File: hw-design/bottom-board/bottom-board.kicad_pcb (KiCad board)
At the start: 2 copper layers, 172 x 140.5 mm, 257 parts, among them J1 JACK_TRS_6PINS, J2 JACK_TRS_6PINS, J3 JACK_TRS_6PINS, J4 JACK_TRS_6PINS, J5 JACK_TRS_6PINS, J6 RJ45_LEDS, K1 IM06TS, K2 IM06TS, P1 USB_B, P2 USB_A, P3 DIN_5, P4 DIN_5, P5 BARREL_JACK, P6 HMI_POWER, P7 SD_CARD, P8 HMI_DATA, P9 SERIAL_DEBUG, Q1 2N7002, Q10 2N7002, Q12 2N7002, Q13 2N7002, Q14 BSS84, Q15 BSS84, Q2 2N7002, Q3 J112, Q4 J112, Q5 J112, Q6 J112, Q7 2N7002, Q8 2N7002, Q9 2N7002, SW1 SW_PUSH, U1 MURATA 5V, U10 RT9701, U11 6N137S, U12 ISL83491, U2 NCP1117DT50G, U3 CS4245, U4 AT24CS08-STUM, U5 Core_AW204x, U6 LM4562, U7 LM4562, U8 LM4562, U9 LM4811

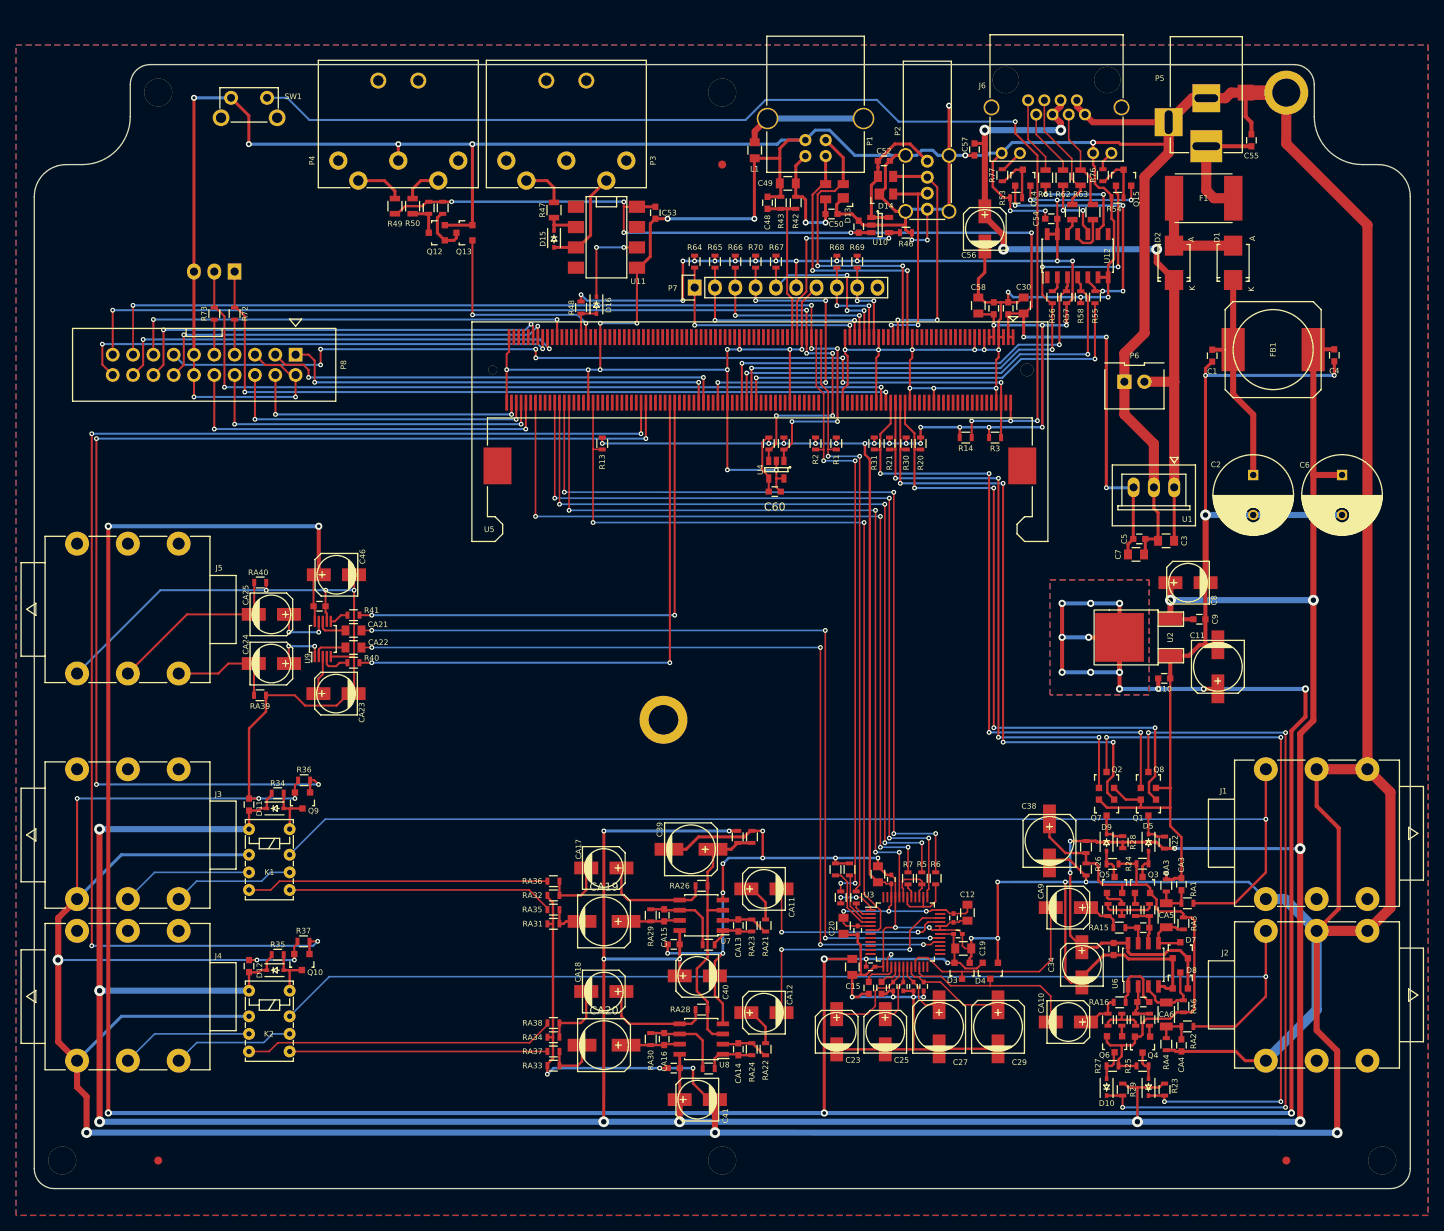
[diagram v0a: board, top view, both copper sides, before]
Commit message: Changed SODIM to Marsboard header + added liniar regulator for audio codec
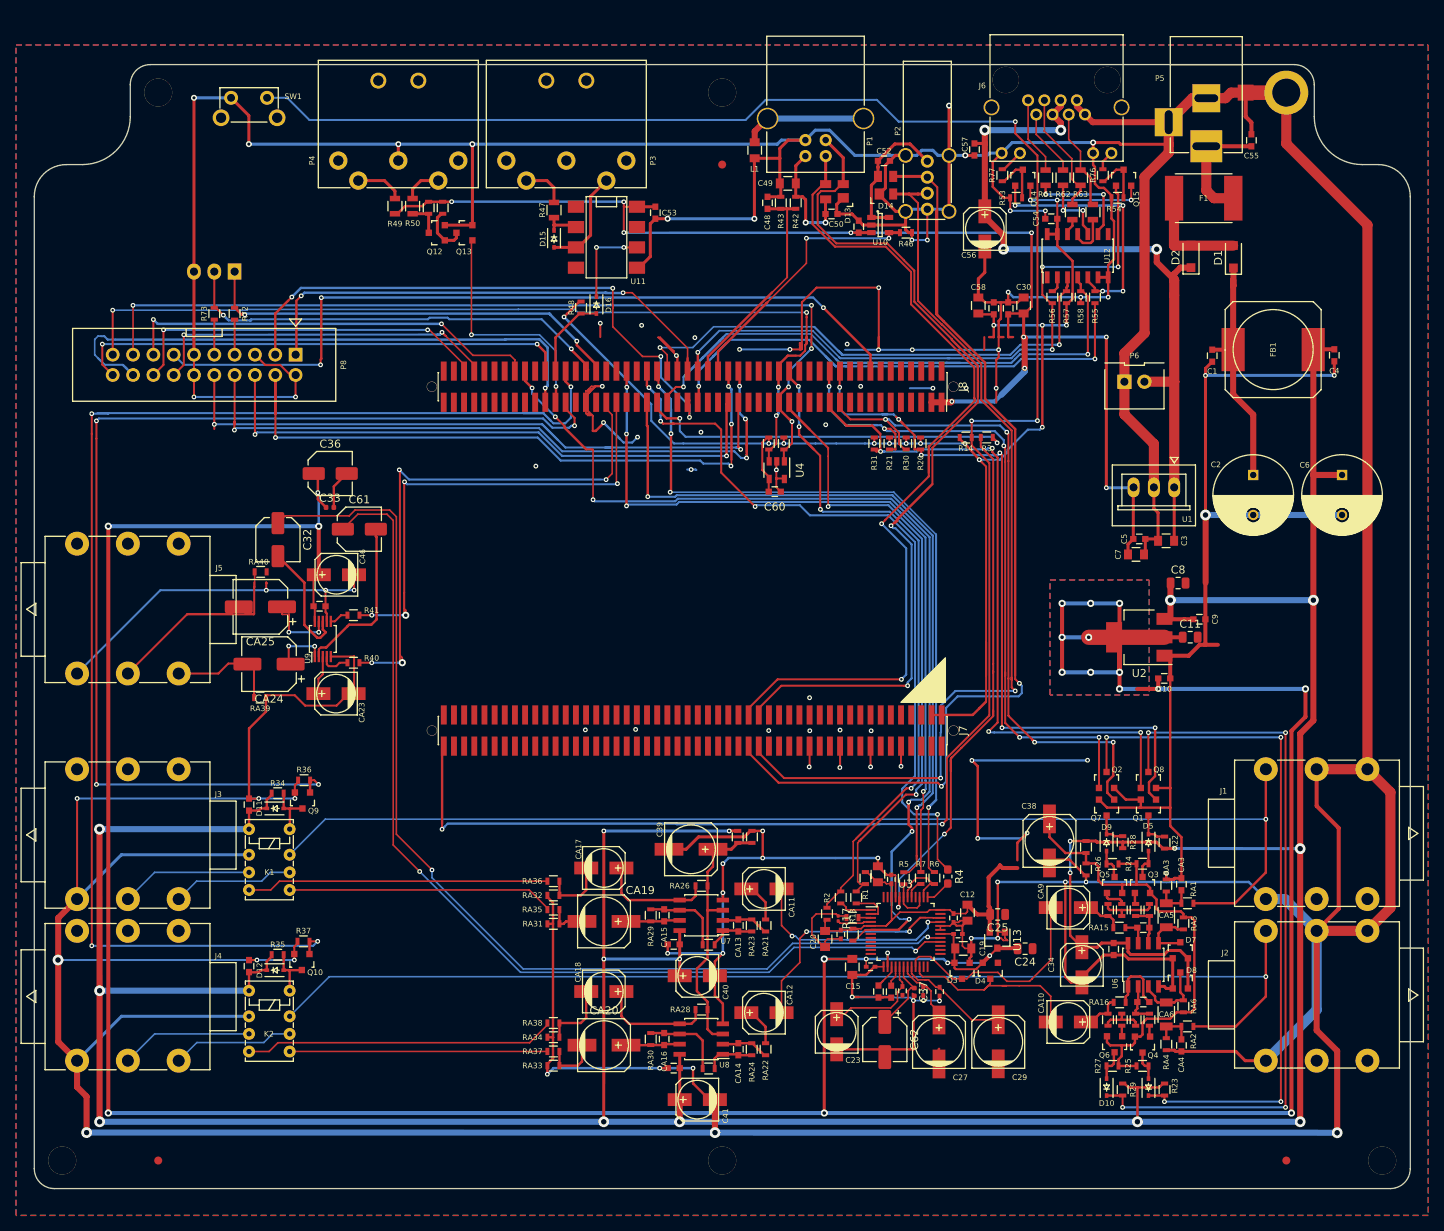
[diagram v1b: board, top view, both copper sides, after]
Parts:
- removed CA21, CA22: 1uF, Capacitors_SMD:C_0805
- removed H6: Standoff, footprints:9774027151R
- removed P7: SD_CARD, Pin_Headers:Pin_Header_Straight_1x10
- removed R11, R64, R65, R66, R67, R68, R69, R70: 10k, Resistors_SMD:R_0603
- removed U5: Core_AW204x, footprints:Socket_SODIMM_DDR3_TE_2013289
- added C32: 10uF, Capacitor_SMD:C_Elec_5x5.4, F.Cu at (90.5, 79.0)
- added C33: 100nF, Capacitor_SMD:C_0402_1005Metric, F.Cu at (97.0, 74.9)
- added C36: 10uF, Capacitor_SMD:C_Elec_5x5.4, F.Cu at (97.1, 70.7)
- added C37: 100nF, Capacitor_SMD:C_0402_1005Metric, F.Cu at (170.1, 135.5)
- added C61: 10uF, Capacitor_SMD:C_Elec_5x5.4, F.Cu at (100.7, 77.6)
- added C62: 10uF, Capacitor_SMD:CP_Elec_5x5.3, F.Cu at (166.4, 141.4)
- added G***: LOGO, footprints:mod-logo, B.Cu at (145.7, 91.9)
- added J7: Conn_02x50_Odd_Even, footprints-local:Pin_Header_Straight_2x50_Pitch1.27mm_SMD, F.Cu at (142.4, 102.8)
- added J8: Conn_02x50_Odd_Even, footprints-local:Pin_Header_Straight_2x50_Pitch1.27mm_SMD, F.Cu at (142.4, 59.8)
- added R17: 10k, Resistor_SMD:R_0201_0603Metric, F.Cu at (160.6, 126.3)
- added R4: 22R, Resistor_SMD:R_0603_1608Metric_Pad1.05x0.95mm_HandSolder, F.Cu at (174.3, 121.1)
- added U13: AP2120N-3.3, Package_TO_SOT_SMD:SOT-23, F.Cu at (180.5, 129.0)
- C11: value 100uF -> 10uF; footprint Capacitors_SMD:c_elec_6.3x5.3 -> Capacitor_SMD:C_0805_2012Metric
- C2, C6: value 1000uF -> 2200uF
- C24: value 100nF -> 1uF; footprint Capacitors_SMD:C_0402 -> Capacitor_SMD:C_0805_2012Metric
- C25, C8: footprint Capacitors_SMD:c_elec_5x5.3 -> Capacitor_SMD:C_0805_2012Metric
- CA24, CA25: value 10uF -> 100uF; footprint Capacitors_SMD:c_elec_5x5.3 -> Capacitor_SMD:CP_Elec_6.3x7.7
- D1, D2: value B130LB -> MBR230; footprint Diodes_SMD:Diode-SMB_Standard -> Diode_SMD:D_SOD-123F
- FB1: value 100uH -> 1mH
- R10, R9: value 100R -> 22R
- R3: value 10k -> 22R
- U2: value NCP1117DT50G -> LD1117S50TR_SOT223; footprint SMD_Packages:DPAK-2 -> Package_TO_SOT_SMD:SOT-223-3_TabPin2
- U3: footprint Housings_QFP:LQFP-48_7x7mm_Pitch0.5mm -> Package_QFP:LQFP-48_7x7mm_P0.5mm
- U4: footprint Housings_SOT-23_SOT-143_TSOT-6:SOT-23-5 -> Package_TO_SOT_SMD:SOT-23-5
- moved R13 68.9 mm to (162.4, 128.3), turned to 270 degrees
- moved R2 58.8 mm to (159.2, 125.7), turned to 270 degrees
- moved R1 54.4 mm to (164.0, 121.3)
- moved C25 20.3 mm to (180.5, 125.8), turned to 180 degrees
- moved C24 15.9 mm to (183.9, 130.1), turned to 180 degrees
- moved R12 6.40 mm to (162.4, 126.2), turned to 0 degrees
- moved C11 5.07 mm to (204.6, 91.1), turned to 0 degrees
- moved U2 3.88 mm to (198.2, 91.2), turned to 180 degrees
- moved CA1 2.84 mm to (167.2, 135.5)
- moved C20 2.83 mm to (158.9, 128.9)
- moved D2 2.27 mm to (204.7, 43.5)
- moved R5 2.25 mm to (168.8, 121.3)
- moved C21 2.17 mm to (160.9, 128.3)
- moved C28 2.09 mm to (173.2, 135.4)
- moved C27 1.89 mm to (173.2, 141.7)
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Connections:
- C12 pad 2: +3V3 -> +3.3VA
- C14 pad 2: +3V3 -> +3.3VA
- C16 pad 2: +3V3 -> +3.3VA
- C18 pad 1: +3V3 -> +3.3VA
- C20 pad 2: +3V3 -> +3.3VA
- C21 pad 2: +3V3 -> +3.3VA
- C24 pad 1: Net-(C24-Pad1) -> GNDA
- C24 pad 2: GNDA -> +5VA
- C25 pad 1: Net-(C24-Pad1) -> GNDA
- C25 pad 2: GNDA -> +3.3VA
- R1 pad 2: +3V3 -> +3.3VA
- R13 pad 1: CODEC_~RESET -> +3.3VA
- R13 pad 2: +3V3 -> CODEC_~RESET
- R2 pad 2: +3V3 -> +3.3VA
- R3 pad 1: +3V3 -> Net-(R3-Pad1)
- R3 pad 2: POWER_BUTTON -> CODEC_I2S_MCLK
- U11 pad 1: (no net) -> Net-(U11-Pad1)
- U11 pad 4: (no net) -> Net-(U11-Pad4)
- U3 pad 15: Net-(CA1-Pad1) -> Net-(CA2-Pad1)
- U3 pad 16: Net-(CA2-Pad1) -> Net-(CA1-Pad1)
- U3 pad 18: Net-(C24-Pad1) -> Net-(C37-Pad1)
- U3 pad 3: Net-(R11-Pad2) -> Net-(R12-Pad2)
- U3 pad 36: +3V3 -> +3.3VA
- U3 pad 37: CODEC_I2S_SDIN -> Net-(R4-Pad2)
- U3 pad 4: Net-(R12-Pad2) -> Net-(R17-Pad2)
- U3 pad 44: CODEC_I2S_MCLK -> Net-(R3-Pad1)
- U3 pad 46: +3V3 -> +3.3VA
- U3 pad 5: +3V3 -> +3.3VA
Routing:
- net UBOOT_BUTTON: track 148.0 -> 280.9 mm, vias 4 -> 5
- net USB_HOST_DM: track 29.7 -> 135.3 mm
- net +3V3: track 292.3 -> 192.7 mm, vias 36 -> 16
- net USB_HOST_DP: track 25.8 -> 116.2 mm
- net USB_DEV_DP: track 38.6 -> 111.0 mm
- net USB_DEV_DM: track 35.3 -> 106.2 mm
- net Net-(R3-Pad1): track 0.00 -> 69.3 mm, vias 0 -> 2
- net CODEC_I2S_MCLK: track 103.1 -> 47.3 mm, vias 4 -> 2
- net HMI_SPI0_MISO: track 35.9 -> 83.2 mm, vias 2 -> 4
- net +3.3VA: track 0.00 -> 46.4 mm
- net CLI_UART_RX: track 99.1 -> 55.7 mm
- net GNDA: track 1685.4 -> 1642.0 mm, vias 77 -> 91
- net CLI_UART_TX: track 97.2 -> 53.9 mm
- net HMI_SPI0_CLK: track 44.7 -> 85.1 mm, vias 2 -> 4
- net SD0_DETECT: track 39.1 -> 0.00 mm, vias 4 -> 0
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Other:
- board text added: "MOD Devices GmbH http://moddevices.com MOD Duo - Bottom Board Rev.: 2019.03.28"
- board text removed: "3V3"
- board text removed: "Musical Operating Devices http://moddevices.com MOD Duo - Bottom Board Rev.: 2016.11.29"
- board text removed: "SD_CLK"
- board text removed: "SD_CMD"
- board text removed: "SD_D0"
- board text removed: "SD_D1"
- board text removed: "SD_D2"
- board text removed: "SD_D3"
- board text removed: "SD_DET"

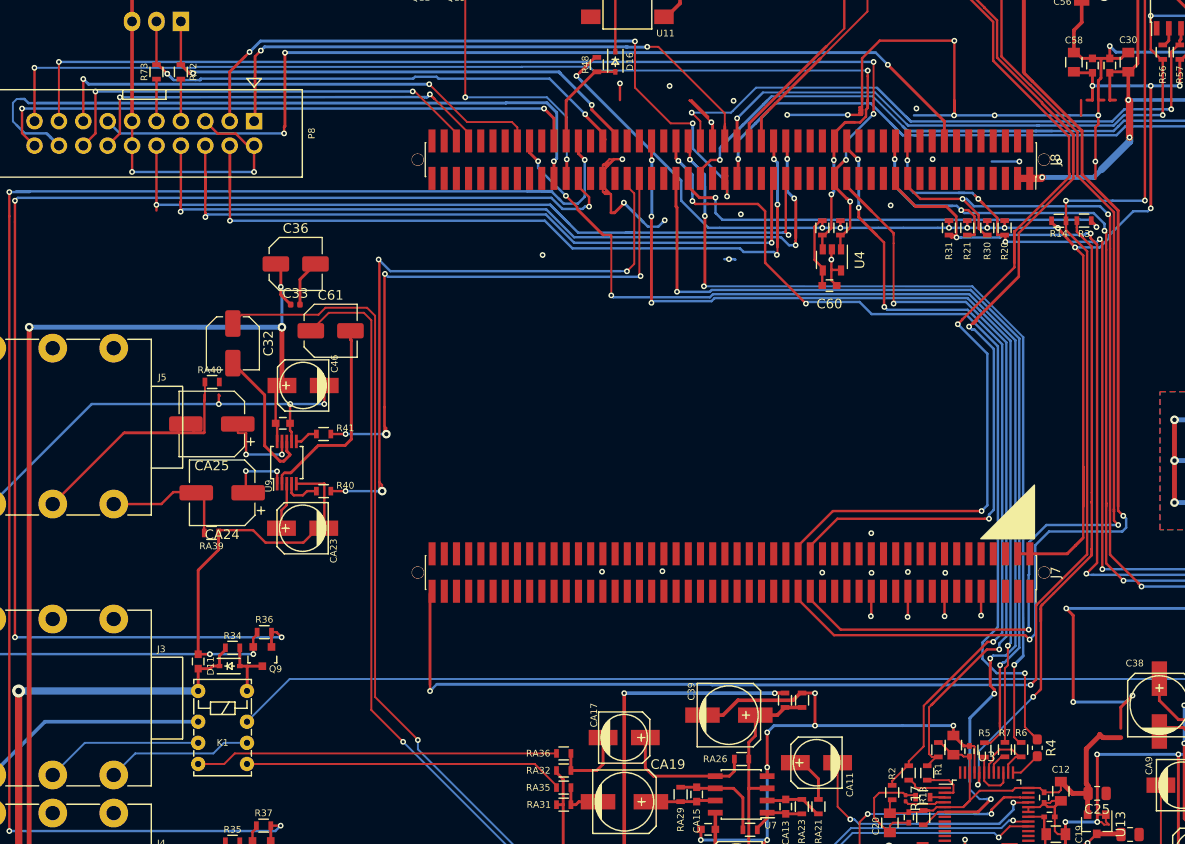
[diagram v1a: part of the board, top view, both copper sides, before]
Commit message: improved routing
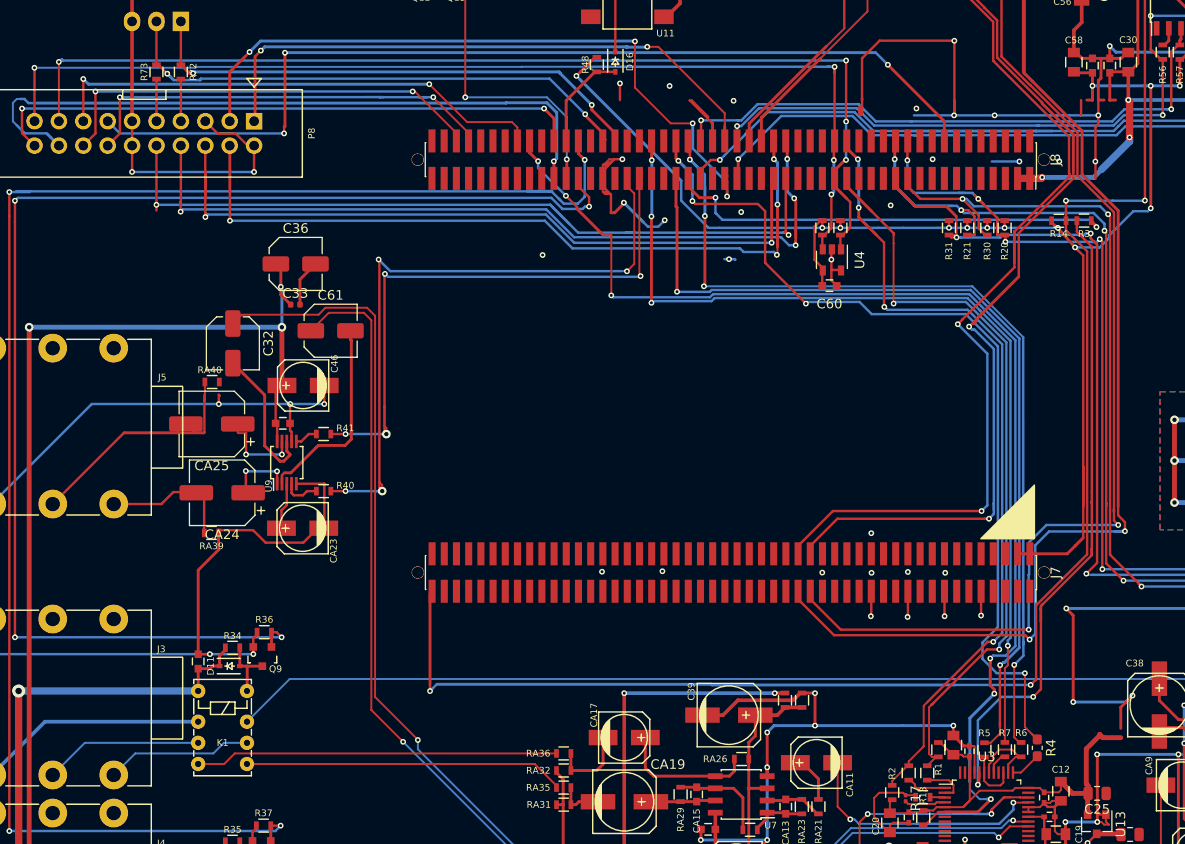
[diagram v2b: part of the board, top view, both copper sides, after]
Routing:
- net CHAIN_UART_TX: track 72.4 -> 63.5 mm
- net CHAIN_UART_RE: track 70.4 -> 62.3 mm
- net GNDA: track 1642.0 -> 1634.4 mm, vias 91 -> 88
- net CHAIN_UART_DE: track 75.7 -> 69.7 mm
- net TWI4_SDA: track 115.5 -> 111.1 mm
- net CODEC_I2S_LRCK: track 94.2 -> 96.5 mm
- net Net-(R3-Pad1): track 69.3 -> 71.6 mm
- net TWI4_SCL: track 113.7 -> 111.7 mm, vias 5 -> 4
- net CHAIN_UART_RX: track 80.8 -> 78.9 mm
- net CODEC_I2S_BCLK: track 128.6 -> 127.5 mm
- net USB_HOST_DM: track 135.3 -> 136.1 mm
- net USB_DEV_DP: track 111.0 -> 111.7 mm
